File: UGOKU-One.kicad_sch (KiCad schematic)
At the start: 82 parts, among them J1 ENC/IO, J10 Conn_01x02, J11 USB_C_Receptacle_USB2.0_16P, J12 Conn_01x02, J2 SERVO, J3 Conn_02x03_Odd_Even, J4 14110213001000, J5 Conn_01x05, J6 Conn_01x02, J7 ENC/IO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

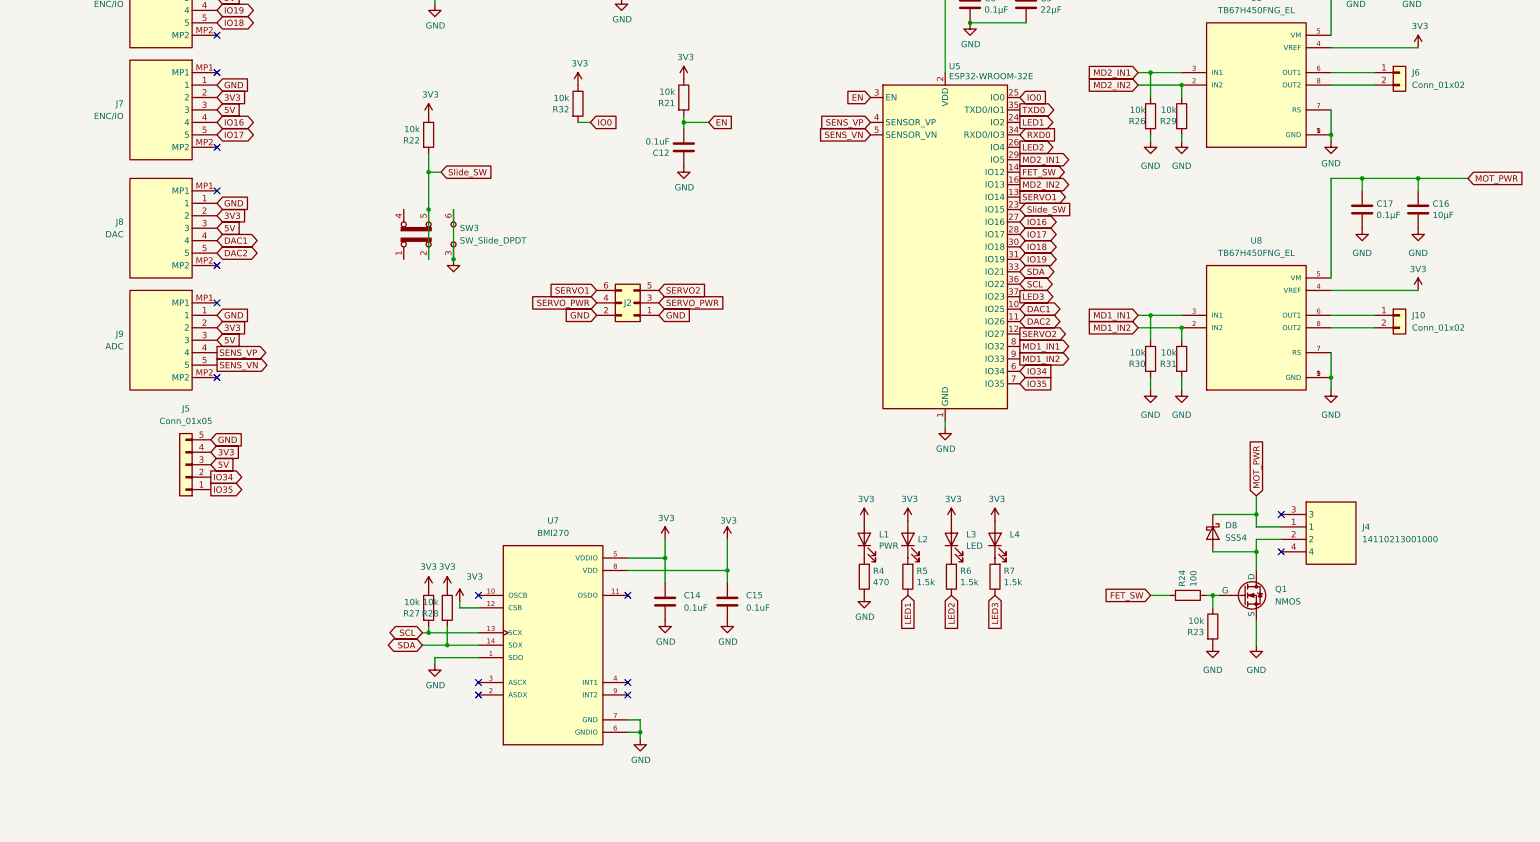
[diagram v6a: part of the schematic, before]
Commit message: change PWR connector SPTAF
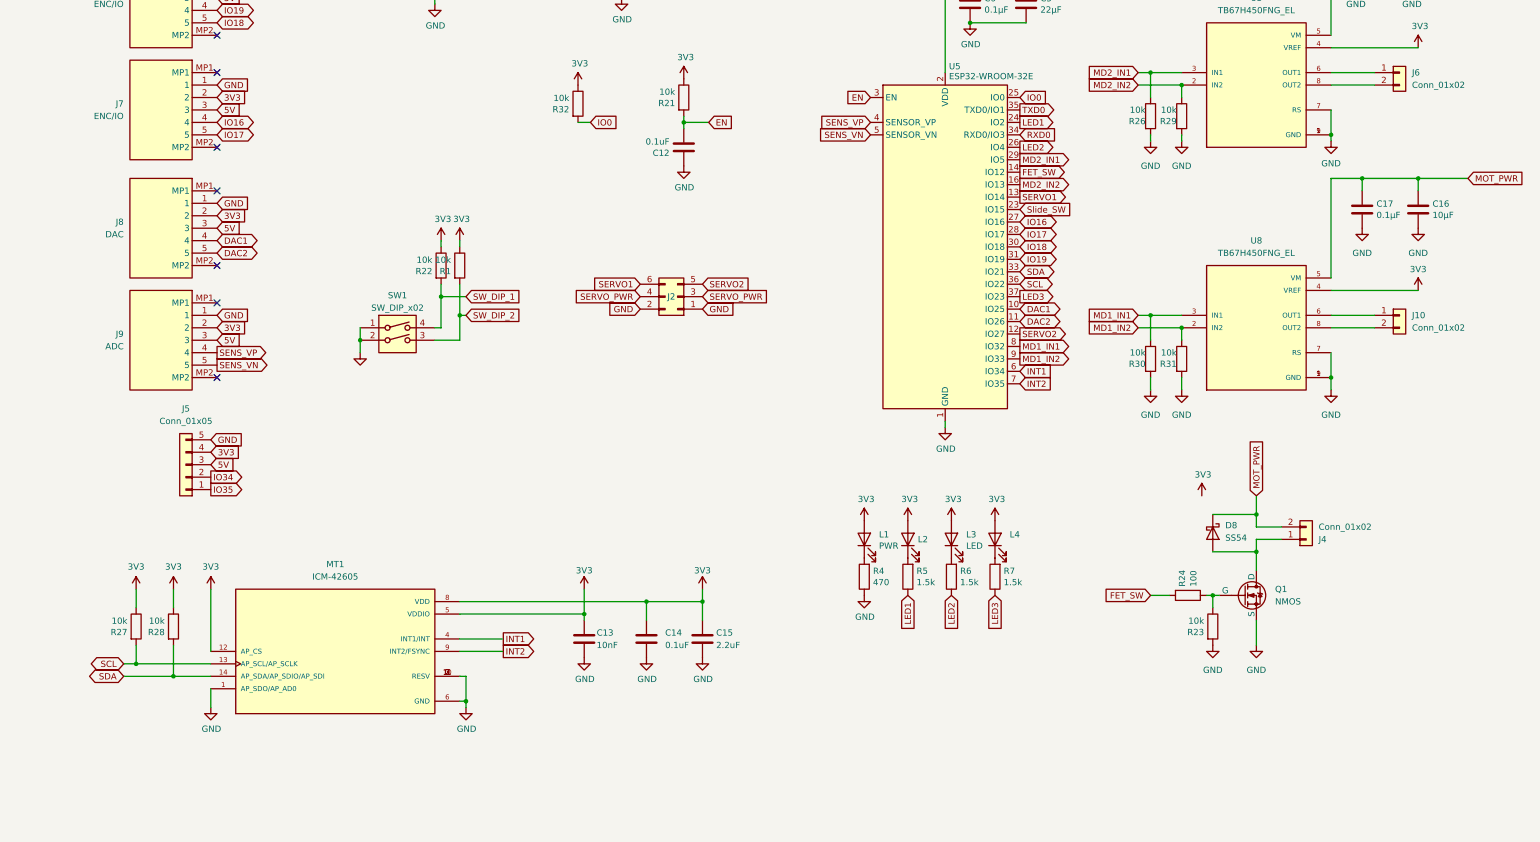
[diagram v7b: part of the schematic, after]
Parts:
- removed J4: 14110213001000, 0_UGOKU-One_Lib:14010213102000, symbol 0_14110213001000:14110213001000
- removed SW3: SW_Slide_DPDT, 0_UGOKU-One_Lib:SSSS213202, symbol Switch:SW_Slide_DPDT
- removed U7: BMI270, 0_UGOKU-One_Lib:XDCR_BMI270, symbol BMI270:BMI270
- added C13: 10nF, Capacitor_SMD:C_0402_1005Metric, symbol Device:C
- added J4: Conn_01x02, 0_UGOKU-One_Lib:PHOENIX_1862411, symbol Connector_Generic:Conn_01x02
- added MT1: ICM-42605, 0_UGOKU-One_Lib:XDCR_ICM-42605, symbol ICM-42605:ICM-42605
- added R1: 10k, Resistor_SMD:R_0402_1005Metric, symbol Device:R
- added SW1: SW_DIP_x02, symbol Switch:SW_DIP_x02
- C15: value 0.1uF -> 2.2uF
- J10, J12, J6: footprint 0_UGOKU-One_Lib:PTS_1.5_2 -> 0_UGOKU-One_Lib:PHOENIX_1862411
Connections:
- net 3V3: now also C13.1, MT1.12 (AP_CS), MT1.5 (VDDIO), MT1.8 (VDD), R1.1
- net GND: now also C13.2, MT1.1 (AP_SDO/AP_AD0), MT1.10 (RESV), MT1.11 (RESV), MT1.2 (RESV), MT1.3 (RESV), MT1.6 (GND), MT1.7 (RESV), SW1.1, SW1.2
- net IO34: no longer U5.6 (IO34)
- net IO35: no longer U5.7 (IO35)
- net MOT_PWR: now also J4.2 (Pin_2)
- net SCL: now also MT1.13 (AP_SCL/AP_SCLK)
- net SDA: now also MT1.14 (AP_SDA/AP_SDIO/AP_SDI)
- net Slide_SW: no longer R22.2
- net at D8.2 (A), Q1.3 (D): now also J4.1 (Pin_1)
- new net INT1: MT1.4 (INT1/INT), U5.6 (IO34)
- new net INT2: MT1.9 (INT2/FSYNC), U5.7 (IO35)
- new net SW_DIP_1: R22.2, SW1.4
- new net SW_DIP_2: R1.2, SW1.3
- no-connect marks 34 -> 26
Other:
- moved on the sheet: C14, C15, J2, R22, R27, R28
